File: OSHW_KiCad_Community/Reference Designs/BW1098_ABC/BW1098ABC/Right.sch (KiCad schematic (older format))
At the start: 13 parts

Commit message: skeleton complete, most footprints assigned, still need to check the transferred ones for dims
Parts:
- C? (x3): footprint (none) -> Capacitor_SMD:C_0201_0603Metric
- C? (x3): footprint (none) -> Capacitor_SMD:C_01005_0402Metric
- FB? (x3): footprint (none) -> Ferrite_THT:LairdTech_28C0236-0JW-10
- R? (x2): footprint (none) -> Resistor_SMD:R_0402_1005Metric
- TP?: value ~ -> TEST_POINT; footprint (none) -> TestPoint:TestPoint_Loop_D1.80mm_Drill1.0mm_Beaded
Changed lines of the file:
@@
 $Descr A4 11693 8268
 encoding utf-8
-Sheet 4 5
+Sheet 4 6
 Title ""
 Date ""
@@
 F 0 "FB?" H 1450 750 60  0000 L BNN
 F 1 "600R/100MHz" H 1450 570 60  0000 L BNN
-F 2 "" H 1450 570 60  0001 C CNN
+F 2 "Ferrite_THT:LairdTech_28C0236-0JW-10" H 1450 570 60  0001 C CNN
 F 3 "" H 1450 570 60  0000 C CNN
 	1    1350 700
@@
 F 0 "FB?" H 1450 1050 60  0000 L BNN
 F 1 "600R/100MHz" H 1450 870 60  0000 L BNN
-F 2 "" H 1450 870 60  0001 C CNN
+F 2 "Ferrite_THT:LairdTech_28C0236-0JW-10" H 1450 870 60  0001 C CNN
 F 3 "" H 1450 870 60  0000 C CNN
 	1    1350 1000
@@
 F 0 "FB?" H 1450 1350 60  0000 L BNN
 F 1 "600R/100MHz" H 1450 1170 60  0000 L BNN
-F 2 "" H 1450 1170 60  0001 C CNN
+F 2 "Ferrite_THT:LairdTech_28C0236-0JW-10" H 1450 1170 60  0001 C CNN
 F 3 "" H 1450 1170 60  0000 C CNN
 	1    1350 1300
@@
 F 0 "C?" V 5960 4760 60  0000 R TNN
 F 1 "0.1uF 0402" V 5860 4760 60  0000 R TNN
-F 2 "" H 5860 4760 60  0001 C CNN
+F 2 "Capacitor_SMD:C_01005_0402Metric" H 5860 4760 60  0001 C CNN
 F 3 "" H 5860 4760 60  0000 C CNN
 F 4 "10V" V -2350 50  60  0001 C CNN "Voltage Rating"
@@
 F 0 "C?" V 4460 4760 60  0000 R TNN
 F 1 "0.1uF 0402" V 4360 4760 60  0000 R TNN
-F 2 "" H 4360 4760 60  0001 C CNN
+F 2 "Capacitor_SMD:C_01005_0402Metric" H 4360 4760 60  0001 C CNN
 F 3 "" H 4360 4760 60  0000 C CNN
 F 4 "10V" V -2350 50  60  0001 C CNN "Voltage Rating"
@@
 F 0 "C?" V 2960 4760 60  0000 R TNN
 F 1 "0.1uF 0402" V 2860 4760 60  0000 R TNN
-F 2 "" H 2860 4760 60  0001 C CNN
+F 2 "Capacitor_SMD:C_01005_0402Metric" H 2860 4760 60  0001 C CNN
 F 3 "" H 2860 4760 60  0000 C CNN
 F 4 "10V" V -2350 50  60  0001 C CNN "Voltage Rating"
@@
 F 0 "C?" V 3560 4760 60  0000 R TNN
 F 1 "10uF 0603" V 3460 4760 60  0000 R TNN
-F 2 "" H 3460 4760 60  0001 C CNN
+F 2 "Capacitor_SMD:C_0201_0603Metric" H 3460 4760 60  0001 C CNN
 F 3 "" H 3460 4760 60  0000 C CNN
 F 4 "10V" V -2350 50  60  0001 C CNN "Voltage Rating"
@@
 F 0 "C?" V 5060 4760 60  0000 R TNN
 F 1 "10uF 0603" V 4960 4760 60  0000 R TNN
-F 2 "" H 4960 4760 60  0001 C CNN
+F 2 "Capacitor_SMD:C_0201_0603Metric" H 4960 4760 60  0001 C CNN
 F 3 "" H 4960 4760 60  0000 C CNN
 F 4 "10V" V -2350 50  60  0001 C CNN "Voltage Rating"
@@
 F 0 "C?" V 6560 4760 60  0000 R TNN
 F 1 "10uF 0603" V 6460 4760 60  0000 R TNN
-F 2 "" H 6460 4760 60  0001 C CNN
+F 2 "Capacitor_SMD:C_0201_0603Metric" H 6460 4760 60  0001 C CNN
 F 3 "" H 6460 4760 60  0000 C CNN
 F 4 "10V" V -2350 50  60  0001 C CNN "Voltage Rating"
@@
 AR Path="/5FF8D40A/6041DE2E" Ref="TP?"  Part="1"
 F 0 "TP?" V 6800 3600 60  0000 L BNN
-F 1 "~" H 6650 3550 50  0001 C CNN
-F 2 "" H 6650 3550 50  0001 C CNN
+F 1 "TEST_POINT" H 6650 3550 50  0001 C CNN
+F 2 "TestPoint:TestPoint_Loop_D1.80mm_Drill1.0mm_Beaded" H 6650 3550 50  0001 C CNN
 F 3 "" H 6650 3550 50  0001 C CNN
 	1    6650 3550
@@
 F 0 "R?" H 7040 2780 60  0000 L BNN
 F 1 "10K 0402" H 7040 2620 60  0000 L BNN
-F 2 "" H 7040 2620 60  0001 C CNN
+F 2 "Resistor_SMD:R_0402_1005Metric" H 7040 2620 60  0001 C CNN
 F 3 "" H 7040 2620 60  0000 C CNN
 	1    6950 2750
@@
 F 0 "R?" H 7040 3180 60  0000 L BNN
 F 1 "0R 0402" H 7040 3020 60  0000 L BNN
-F 2 "" H 7040 3020 60  0001 C CNN
+F 2 "Resistor_SMD:R_0402_1005Metric" H 7040 3020 60  0001 C CNN
 F 3 "" H 7040 3020 60  0000 C CNN
 	1    6950 3150

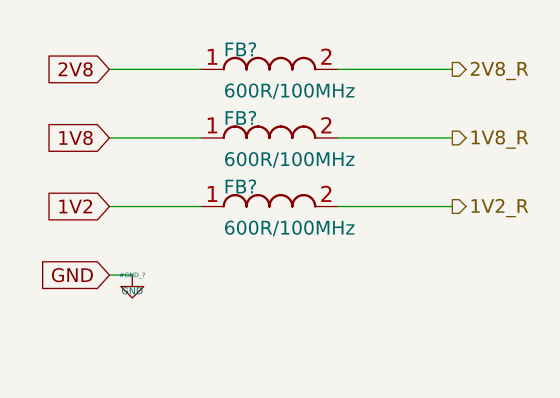
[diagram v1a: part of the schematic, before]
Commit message: schematic edits for BW1098ABC
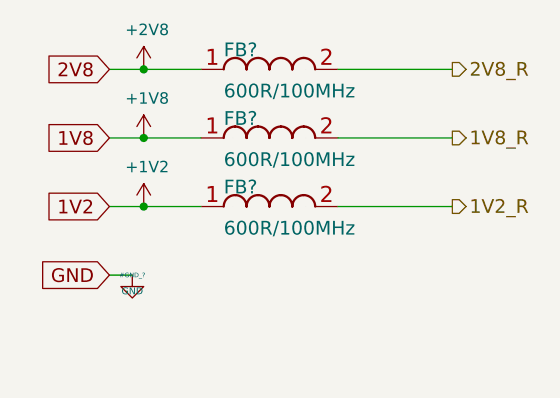
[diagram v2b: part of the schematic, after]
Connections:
- net labels added: +1V2, +1V8, +2V8
- wire segments 60 -> 63
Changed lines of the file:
@@
 	6350 1550 8550 1550
 Wire Wire Line
-	950  1000 1350 1000
-Wire Wire Line
-	950  700  1350 700
-Wire Wire Line
-	950  1300 1350 1300
+	950  1000 1100 1000
+Wire Wire Line
+	950  700  1100 700
+Wire Wire Line
+	950  1300 1100 1300
 Text HLabel 2450 700  2    60   Output ~ 0
 2V8_R
@@
 Text Notes 6320 5250 0    60   ~ 0
 8
+$Comp
+L power:+1V2 #PWR?
+U 1 1 6001513E
+P 1100 1300
+AR Path="/604AEAFA/6001513E" Ref="#PWR?"  Part="1"
+AR Path="/5FF8D40A/6001513E" Ref="#PWR?"  Part="1"
+F 0 "#PWR?" H 1100 1150 50  0001 C CNN
+F 1 "+1V2" H 1115 1473 50  0000 C CNN
+F 2 "" H 1100 1300 50  0001 C CNN
+F 3 "" H 1100 1300 50  0001 C CNN
+	1    1100 1300
+	1    0    0    -1
+$EndComp
+$Comp
+L power:+1V8 #PWR?
+U 1 1 60015144
+P 1100 1000
+AR Path="/604AEAFA/60015144" Ref="#PWR?"  Part="1"
+AR Path="/5FF8D40A/60015144" Ref="#PWR?"  Part="1"
+F 0 "#PWR?" H 1100 850 50  0001 C CNN
+F 1 "+1V8" H 1115 1173 50  0000 C CNN
+F 2 "" H 1100 1000 50  0001 C CNN
+F 3 "" H 1100 1000 50  0001 C CNN
+	1    1100 1000
+	1    0    0    -1
+$EndComp
+$Comp
+L power:+2V8 #PWR?
+U 1 1 6001514A
+P 1100 700
+AR Path="/604AEAFA/6001514A" Ref="#PWR?"  Part="1"
+AR Path="/5FF8D40A/6001514A" Ref="#PWR?"  Part="1"
+F 0 "#PWR?" H 1100 550 50  0001 C CNN
+F 1 "+2V8" H 1115 873 50  0000 C CNN
+F 2 "" H 1100 700 50  0001 C CNN
+F 3 "" H 1100 700 50  0001 C CNN
+	1    1100 700
+	1    0    0    -1
+$EndComp
+Connection ~ 1100 700
+Wire Wire Line
+	1100 700  1350 700
+Connection ~ 1100 1000
+Wire Wire Line
+	1100 1000 1350 1000
+Connection ~ 1100 1300
+Wire Wire Line
+	1100 1300 1350 1300
 $EndSCHEMATC

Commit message: small stuff
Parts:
- C? (x3): symbol depthAI_sch:GRM188R61A106ME69D -> BW1098ABC-rescue:GRM188R61A106ME69D-depthAI_sch
- C? (x3): symbol depthAI_sch:GRM155R71A104JA01D -> BW1098ABC-rescue:GRM155R71A104JA01D-depthAI_sch
- FB? (x3): symbol depthAI_sch:2508056017Y2 -> BW1098ABC-rescue:2508056017Y2-depthAI_sch
- J?: symbol depthAI_sch:TG161B-201_Connector -> BW1098ABC-rescue:TG161B-201_Connector-depthAI_sch
- R?: symbol depthAI_sch:CRCW04020000Z0ED -> BW1098ABC-rescue:CRCW04020000Z0ED-depthAI_sch
- R?: symbol depthAI_sch:RC0402FR-1310KL -> BW1098ABC-rescue:RC0402FR-1310KL-depthAI_sch
- TP?: symbol depthAI_sch:TEST_POINT -> BW1098ABC-rescue:TEST_POINT-depthAI_sch
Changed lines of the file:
@@
 	1050 1600 950  1600
 $Comp
-L depthAI_sch:2508056017Y2 FB?
+L BW1098ABC-rescue:2508056017Y2-depthAI_sch FB?
 U 1 1 6041DE16
 P 1350 700
@@
 $EndComp
 $Comp
-L depthAI_sch:2508056017Y2 FB?
+L BW1098ABC-rescue:2508056017Y2-depthAI_sch FB?
 U 1 1 6041DE34
 P 1350 1000
@@
 $EndComp
 $Comp
-L depthAI_sch:2508056017Y2 FB?
+L BW1098ABC-rescue:2508056017Y2-depthAI_sch FB?
 U 1 1 6041DE3A
 P 1350 1300
@@
 	2150 7200 5450 7200
 $Comp
-L depthAI_sch:GRM155R71A104JA01D C?
+L BW1098ABC-rescue:GRM155R71A104JA01D-depthAI_sch C?
 U 1 1 6041DE64
 P 5850 4850
@@
 $EndComp
 $Comp
-L depthAI_sch:GRM155R71A104JA01D C?
+L BW1098ABC-rescue:GRM155R71A104JA01D-depthAI_sch C?
 U 1 1 6041DE5D
 P 4350 4850
@@
 $EndComp
 $Comp
-L depthAI_sch:GRM155R71A104JA01D C?
+L BW1098ABC-rescue:GRM155R71A104JA01D-depthAI_sch C?
 U 1 1 6041DE56
 P 2850 4850
@@
 $EndComp
 $Comp
-L depthAI_sch:GRM188R61A106ME69D C?
+L BW1098ABC-rescue:GRM188R61A106ME69D-depthAI_sch C?
 U 1 1 6041DE4F
 P 3450 4850
@@
 $EndComp
 $Comp
-L depthAI_sch:GRM188R61A106ME69D C?
+L BW1098ABC-rescue:GRM188R61A106ME69D-depthAI_sch C?
 U 1 1 6041DE48
 P 4950 4850
@@
 $EndComp
 $Comp
-L depthAI_sch:GRM188R61A106ME69D C?
+L BW1098ABC-rescue:GRM188R61A106ME69D-depthAI_sch C?
 U 1 1 6041DE41
 P 6450 4850
@@
 $EndComp
 $Comp
-L depthAI_sch:TEST_POINT TP?
+L BW1098ABC-rescue:TEST_POINT-depthAI_sch TP?
 U 1 1 6041DE2E
 P 6650 3550
@@
 $EndComp
 $Comp
-L depthAI_sch:RC0402FR-1310KL R?
+L BW1098ABC-rescue:RC0402FR-1310KL-depthAI_sch R?
 U 1 1 6041DE28
 P 6950 2750
@@
 $EndComp
 $Comp
-L depthAI_sch:CRCW04020000Z0ED R?
+L BW1098ABC-rescue:CRCW04020000Z0ED-depthAI_sch R?
 U 1 1 6041DE22
 P 6950 3150
@@
 $EndComp
 $Comp
-L depthAI_sch:TG161B-201_Connector J?
+L BW1098ABC-rescue:TG161B-201_Connector-depthAI_sch J?
 U 1 1 6041DE1C
 P 3750 2550

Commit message: all footprints associated on bw1098abc board except two I need to clarify with Brian. Need to talk to chris about power
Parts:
- C? (x3): footprint Capacitor_SMD:C_0201_0603Metric -> Capacitor_SMD:C_0603_1608Metric
- C? (x3): footprint Capacitor_SMD:C_01005_0402Metric -> Capacitor_SMD:C_0402_1005Metric
- FB? (x3): footprint Ferrite_THT:LairdTech_28C0236-0JW-10 -> OSHW_LuxonisMaster_20201223:2508056017Y2
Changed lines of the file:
@@
 F 0 "FB?" H 1450 750 60  0000 L BNN
 F 1 "600R/100MHz" H 1450 570 60  0000 L BNN
-F 2 "Ferrite_THT:LairdTech_28C0236-0JW-10" H 1450 570 60  0001 C CNN
+F 2 "OSHW_LuxonisMaster_20201223:2508056017Y2" H 1450 570 60  0001 C CNN
 F 3 "" H 1450 570 60  0000 C CNN
 	1    1350 700
@@
 F 0 "FB?" H 1450 1050 60  0000 L BNN
 F 1 "600R/100MHz" H 1450 870 60  0000 L BNN
-F 2 "Ferrite_THT:LairdTech_28C0236-0JW-10" H 1450 870 60  0001 C CNN
+F 2 "OSHW_LuxonisMaster_20201223:2508056017Y2" H 1450 870 60  0001 C CNN
 F 3 "" H 1450 870 60  0000 C CNN
 	1    1350 1000
@@
 F 0 "FB?" H 1450 1350 60  0000 L BNN
 F 1 "600R/100MHz" H 1450 1170 60  0000 L BNN
-F 2 "Ferrite_THT:LairdTech_28C0236-0JW-10" H 1450 1170 60  0001 C CNN
+F 2 "OSHW_LuxonisMaster_20201223:2508056017Y2" H 1450 1170 60  0001 C CNN
 F 3 "" H 1450 1170 60  0000 C CNN
 	1    1350 1300
@@
 F 0 "C?" V 5960 4760 60  0000 R TNN
 F 1 "0.1uF 0402" V 5860 4760 60  0000 R TNN
-F 2 "Capacitor_SMD:C_01005_0402Metric" H 5860 4760 60  0001 C CNN
+F 2 "Capacitor_SMD:C_0402_1005Metric" H 5860 4760 60  0001 C CNN
 F 3 "" H 5860 4760 60  0000 C CNN
 F 4 "10V" V -2350 50  60  0001 C CNN "Voltage Rating"
@@
 F 0 "C?" V 4460 4760 60  0000 R TNN
 F 1 "0.1uF 0402" V 4360 4760 60  0000 R TNN
-F 2 "Capacitor_SMD:C_01005_0402Metric" H 4360 4760 60  0001 C CNN
+F 2 "Capacitor_SMD:C_0402_1005Metric" H 4360 4760 60  0001 C CNN
 F 3 "" H 4360 4760 60  0000 C CNN
 F 4 "10V" V -2350 50  60  0001 C CNN "Voltage Rating"
@@
 F 0 "C?" V 2960 4760 60  0000 R TNN
 F 1 "0.1uF 0402" V 2860 4760 60  0000 R TNN
-F 2 "Capacitor_SMD:C_01005_0402Metric" H 2860 4760 60  0001 C CNN
+F 2 "Capacitor_SMD:C_0402_1005Metric" H 2860 4760 60  0001 C CNN
 F 3 "" H 2860 4760 60  0000 C CNN
 F 4 "10V" V -2350 50  60  0001 C CNN "Voltage Rating"
@@
 F 0 "C?" V 3560 4760 60  0000 R TNN
 F 1 "10uF 0603" V 3460 4760 60  0000 R TNN
-F 2 "Capacitor_SMD:C_0201_0603Metric" H 3460 4760 60  0001 C CNN
+F 2 "Capacitor_SMD:C_0603_1608Metric" H 3460 4760 60  0001 C CNN
 F 3 "" H 3460 4760 60  0000 C CNN
 F 4 "10V" V -2350 50  60  0001 C CNN "Voltage Rating"
@@
 F 0 "C?" V 5060 4760 60  0000 R TNN
 F 1 "10uF 0603" V 4960 4760 60  0000 R TNN
-F 2 "Capacitor_SMD:C_0201_0603Metric" H 4960 4760 60  0001 C CNN
+F 2 "Capacitor_SMD:C_0603_1608Metric" H 4960 4760 60  0001 C CNN
 F 3 "" H 4960 4760 60  0000 C CNN
 F 4 "10V" V -2350 50  60  0001 C CNN "Voltage Rating"
@@
 F 0 "C?" V 6560 4760 60  0000 R TNN
 F 1 "10uF 0603" V 6460 4760 60  0000 R TNN
-F 2 "Capacitor_SMD:C_0201_0603Metric" H 6460 4760 60  0001 C CNN
+F 2 "Capacitor_SMD:C_0603_1608Metric" H 6460 4760 60  0001 C CNN
 F 3 "" H 6460 4760 60  0000 C CNN
 F 4 "10V" V -2350 50  60  0001 C CNN "Voltage Rating"

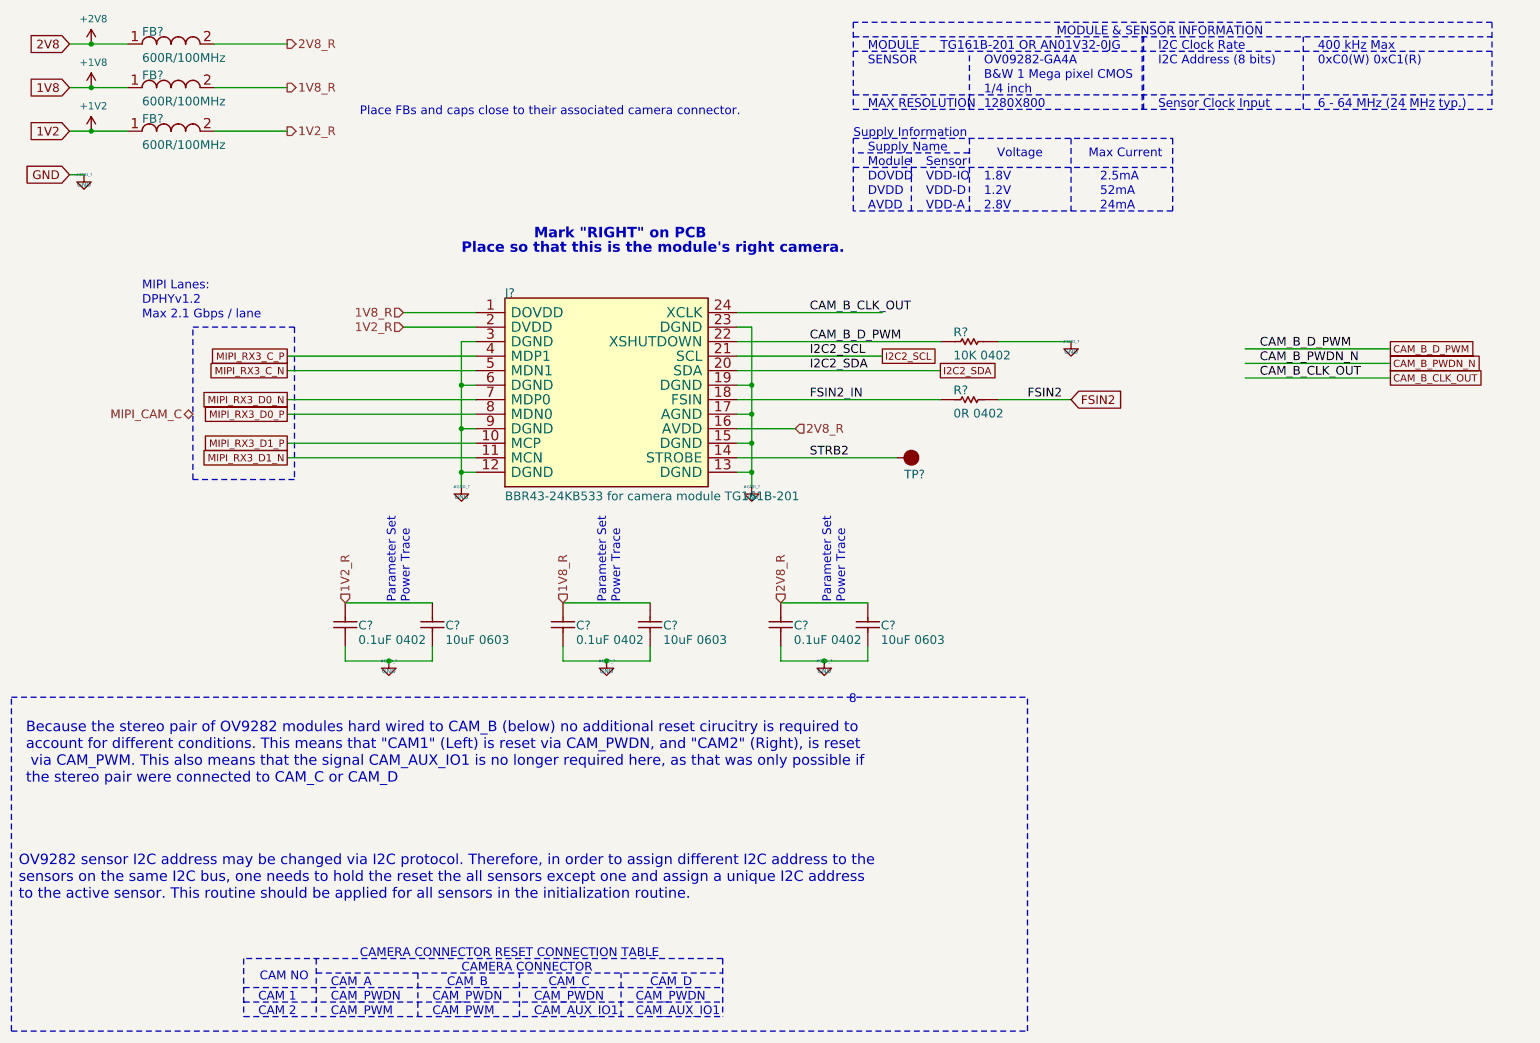
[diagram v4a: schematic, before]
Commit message: added busses, fixed hierarchical labeling, just need to fix an erc thing with my buses then itll pass
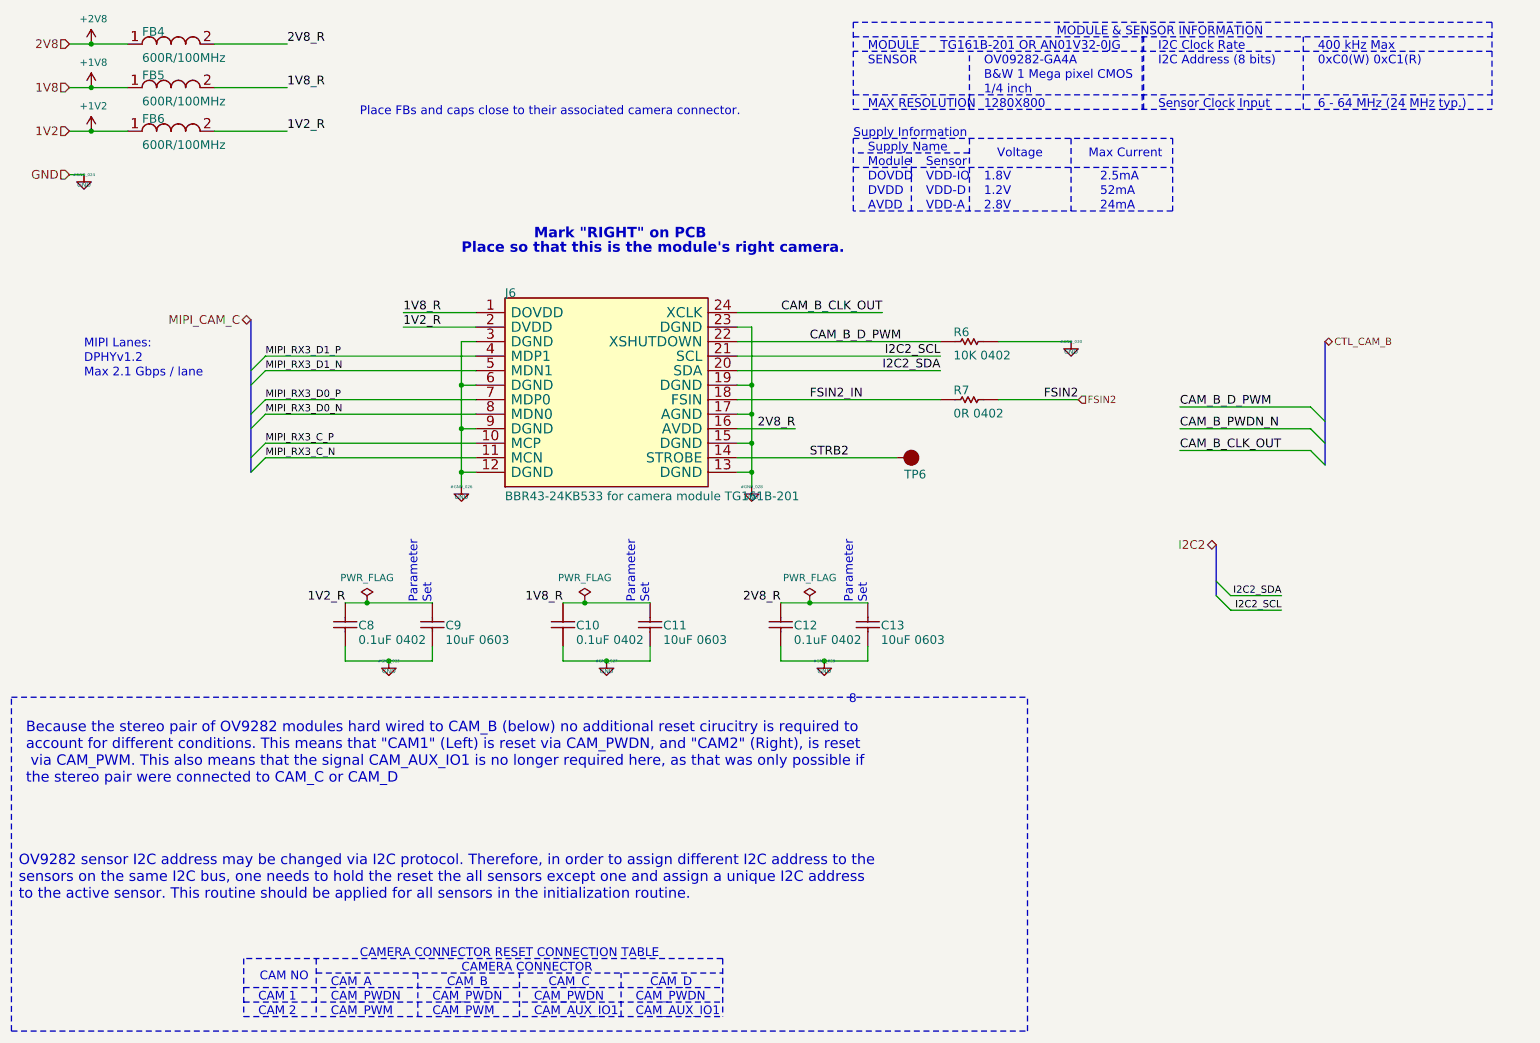
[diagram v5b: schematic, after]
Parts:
- gave numbers to parts that had none: 13
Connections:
- net labels added: CTL_CAM_B, I2C2
- wire segments 63 -> 68
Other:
- note added: "Parameter \nSet\n"
- note removed: "Parameter Set\nPower Trace"
